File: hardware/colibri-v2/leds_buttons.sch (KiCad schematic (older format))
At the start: 39 parts, among them SW1 SW_PUSH, SW3 SW_PUSH, SW5 SW_PUSH

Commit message: Re-annotated schematic
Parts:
- gave numbers to parts that had none: 24
- renumbered C30 to C29, R35 to R36, R36 to R37, R37 to R38, R38 to R39

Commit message: Associated footprints for R and some of the C
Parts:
- C27, C28, C29, C30, C31, C32: footprint (none) -> Capacitors_SMD:C_0603
- R18, R19, R20, R21, R22, R23, R24, R25, R26, R27, R28, R29, R30, R31, R32, R33, R34, R35, R36, R37, R38, R39: footprint (none) -> Resistors_SMD:R_0603

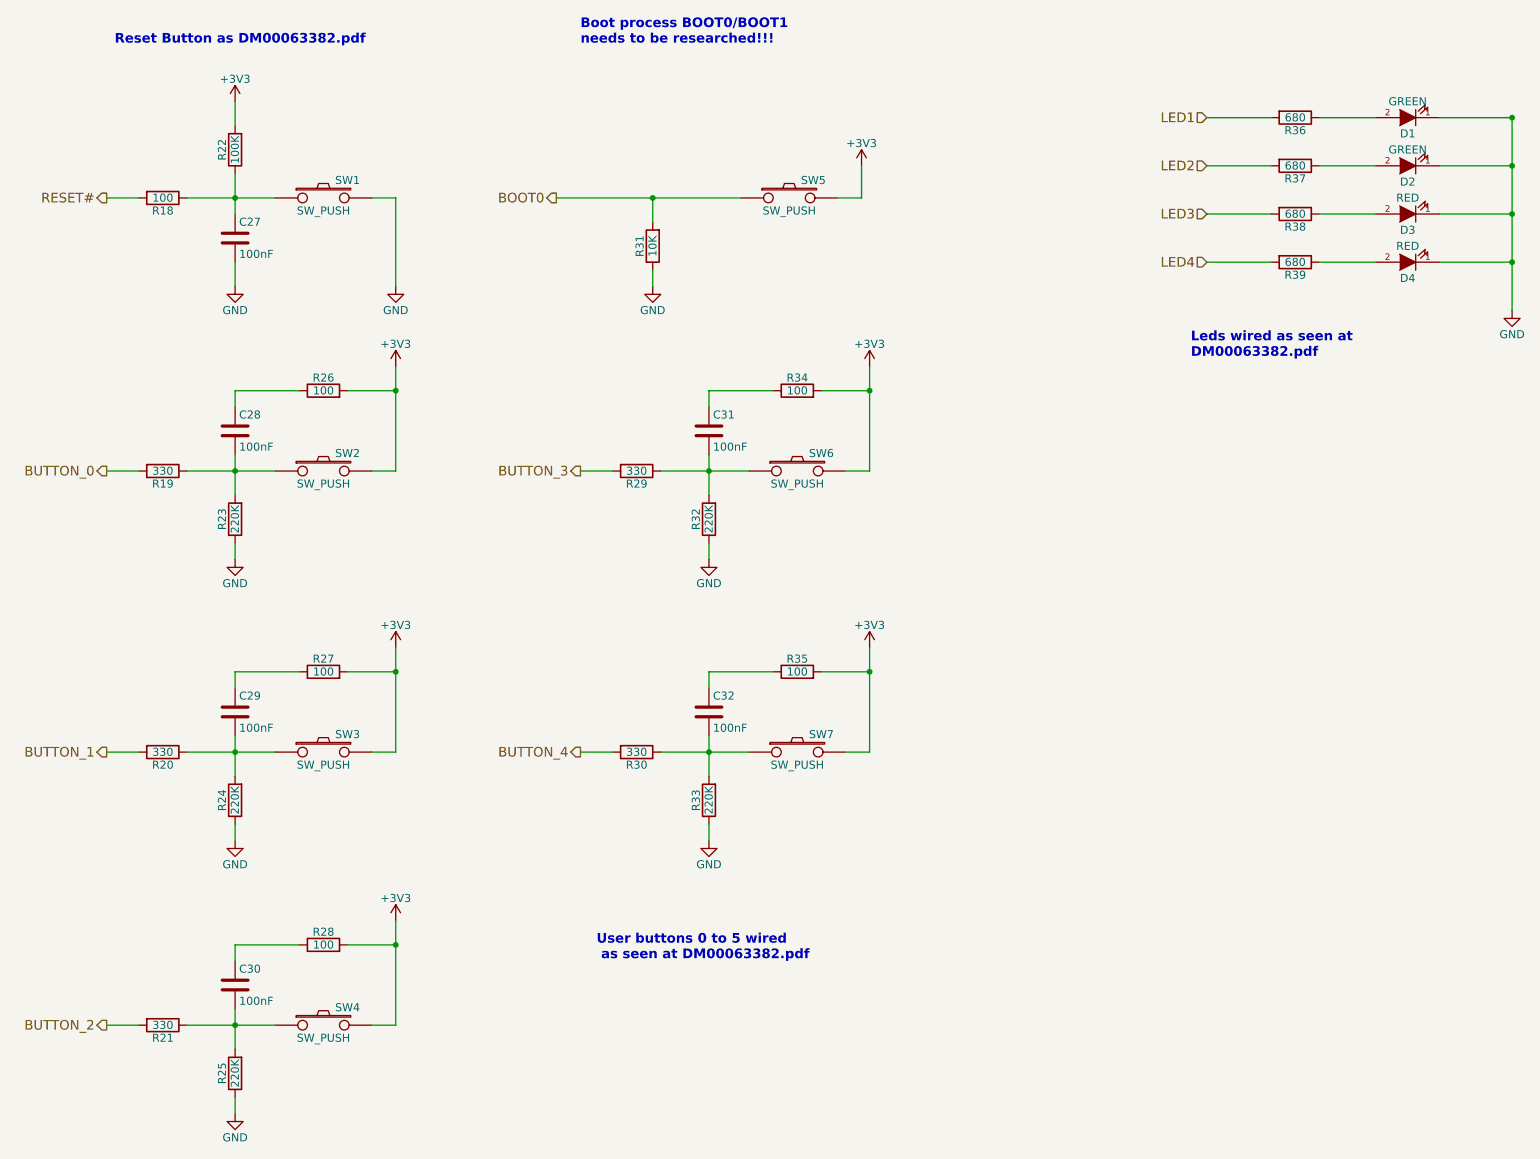
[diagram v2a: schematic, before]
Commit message: Work on JTAG and buttons sheets
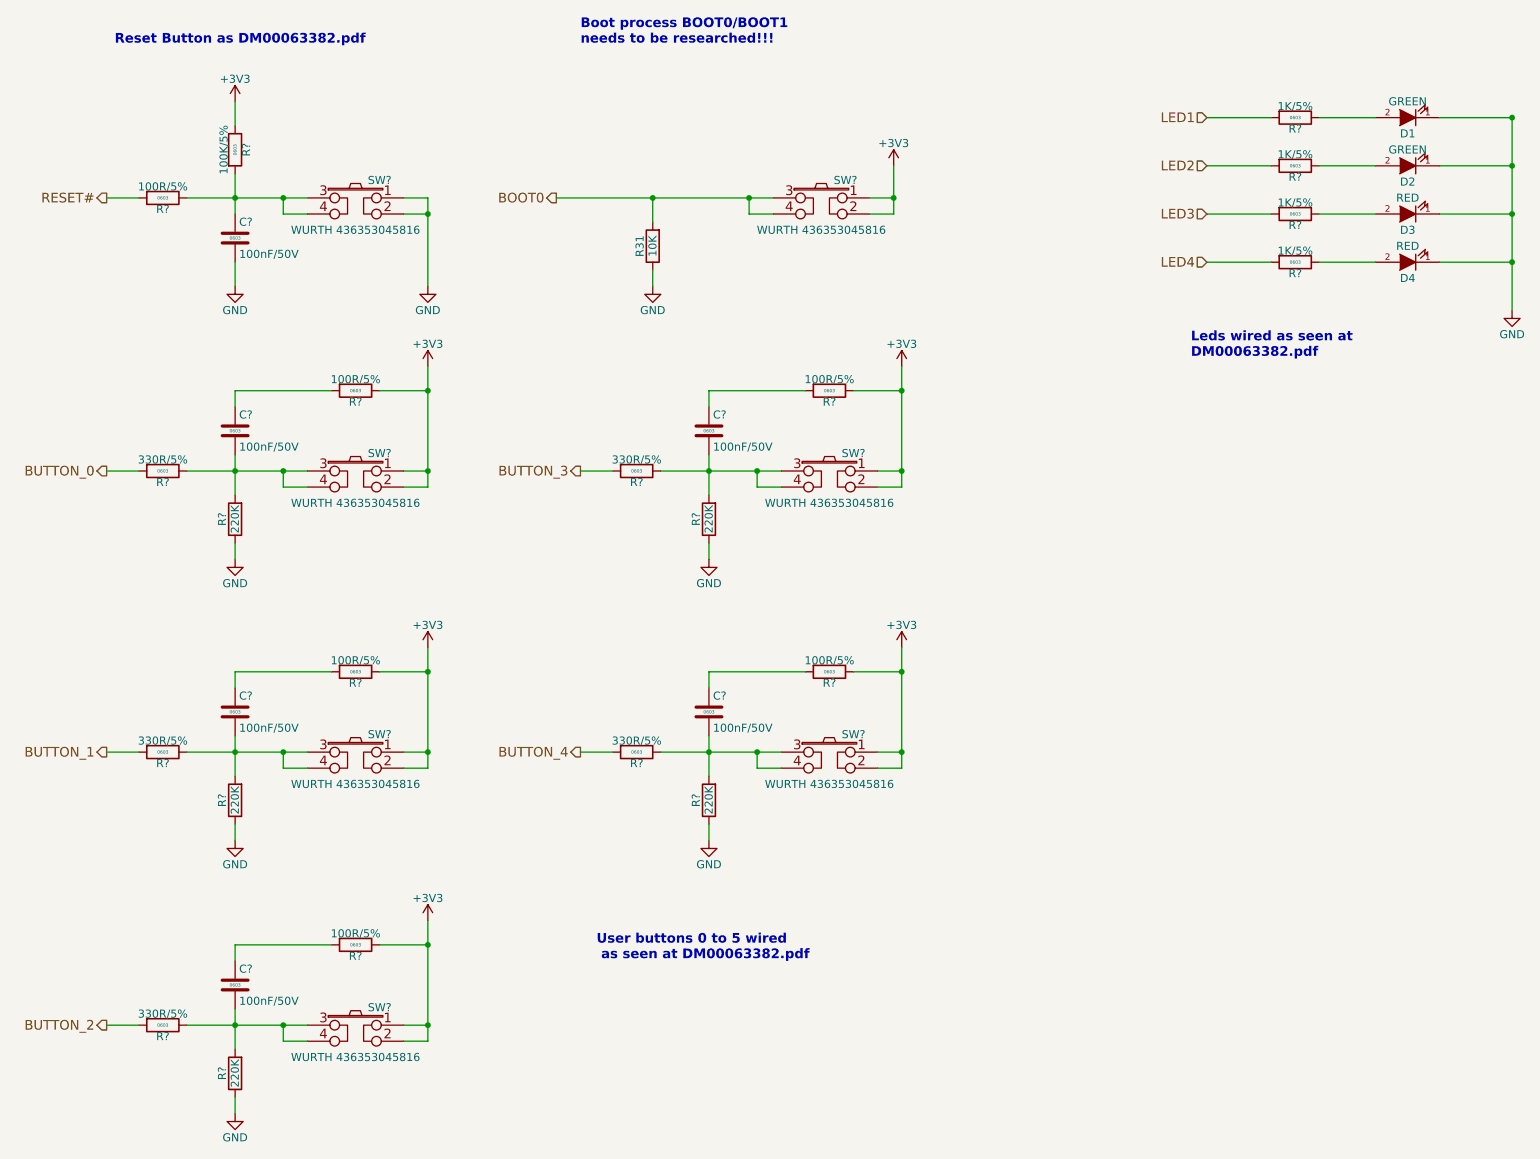
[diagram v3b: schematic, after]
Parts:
- removed C27, C28, C29, C30, C31, C32: 100nF, Capacitors_SMD:C_0603, symbol C
- removed R18, R26, R27, R28, R34, R35: 100, Resistors_SMD:R_0603, symbol R
- removed R19, R20, R21, R29, R30: 330, Resistors_SMD:R_0603, symbol R
- removed R22: 100K, Resistors_SMD:R_0603, symbol R
- removed R23, R24, R25, R32, R33: 220K, Resistors_SMD:R_0603, symbol R
- removed R36, R37, R38, R39: 680, Resistors_SMD:R_0603, symbol R
- removed SW1, SW2, SW3, SW4, SW5, SW6, SW7: SW_PUSH, symbol SW_PUSH
- added C? (x6): 100nF/50V, Capacitors_SMD:C_0603, symbol C_SMT
- added R?: 100K/5%, Resistors_SMD:R_0603, symbol R_SMT
- added R? (x6): 100R/5%, Resistors_SMD:R_0603, symbol R_SMT
- added R? (x5): 220K, Resistors_SMD:R_0603, symbol R
- added R? (x5): 330R/5%, Resistors_SMD:R_0603, symbol R_SMT
- added R? (x4): 1K/5%, Resistors_SMD:R_0603, symbol R_SMT
- added SW? (x7): WURTH 436353045816, symbol SW_PUSH_TACKTILE
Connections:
- net +3V3: now also R?.1, R?.1, R?.1, R?.1, R?.1, R?.1, SW?.1, SW?.1, SW?.1, SW?.1, SW?.1, SW?.1, SW?.2, SW?.2, SW?.2, SW?.2, SW?.2, SW?.2
- net BOOT0: now also SW?.3, SW?.4
- net BUTTON_0: now also R?.2
- net BUTTON_1: now also R?.2
- net BUTTON_2: now also R?.2
- net BUTTON_3: now also R?.2
- net BUTTON_4: now also R?.2
- net GND: now also C?.2, R?.1, R?.1, R?.1, R?.1, R?.1, SW?.1, SW?.2
- net LED1: now also R?.2
- net LED2: now also R?.2
- net LED3: now also R?.2
- net LED4: now also R?.2
- net RESET#: now also R?.2
- net at D1.2 (A): now also R?.1
- net at D2.2 (A): now also R?.1
- net at D3.2 (A): now also R?.1
- net at D4.2 (A): now also R?.1
- new net: C?.1, R?.1, R?.2, SW?.3, SW?.4
- new net: C?.2, R?.1, R?.2, SW?.3, SW?.4 (x5)
- new net: C?.1, R?.2 (x5)

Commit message: Work on cortex USB connection.
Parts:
- renumbered D1 to D?, D2 to D?, D3 to D?, D4 to D?, R31 to R?
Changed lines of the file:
@@
 RESET#
 $Comp
-L LED D1
+L LED D?
 U 1 1 55862ED2
 P 9450 1200
-F 0 "D1" H 9450 1300 50  0000 C CNN
+F 0 "D?" H 9450 1300 50  0000 C CNN
 F 1 "GREEN" H 9450 1100 50  0000 C CNN
 F 2 "" H 9450 1200 60  0001 C CNN
@@
 $EndComp
 $Comp
-L LED D2
+L LED D?
 U 1 1 55863115
 P 9450 1500
-F 0 "D2" H 9450 1600 50  0000 C CNN
+F 0 "D?" H 9450 1600 50  0000 C CNN
 F 1 "GREEN" H 9450 1400 50  0000 C CNN
 F 2 "" H 9450 1500 60  0001 C CNN
@@
 $EndComp
 $Comp
-L LED D3
+L LED D?
 U 1 1 55863212
 P 9450 1800
-F 0 "D3" H 9450 1900 50  0000 C CNN
+F 0 "D?" H 9450 1900 50  0000 C CNN
 F 1 "RED" H 9450 1700 50  0000 C CNN
 F 2 "" H 9450 1800 60  0001 C CNN
@@
 $EndComp
 $Comp
-L LED D4
+L LED D?
 U 1 1 558632D0
 P 9450 2100
-F 0 "D4" H 9450 2200 50  0000 C CNN
+F 0 "D?" H 9450 2200 50  0000 C CNN
 F 1 "RED" H 9450 2000 50  0000 C CNN
 F 2 "" H 9450 2100 60  0001 C CNN
@@
 LED4
 $Comp
-L GND #PWR018
+L GND #PWR?
 U 1 1 56074E25
 P 3350 2250
-F 0 "#PWR018" H 3350 2000 50  0001 C CNN
+F 0 "#PWR?" H 3350 2000 50  0001 C CNN
 F 1 "GND" H 3350 2100 50  0000 C CNN
 F 2 "" H 3350 2250 60  0000 C CNN
@@
 BOOT0
 $Comp
-L R R31
+L R R?
 U 1 1 5622C644
 P 4750 2000
-F 0 "R31" V 4830 2000 50  0000 C CNN
+F 0 "R?" V 4830 2000 50  0000 C CNN
 F 1 "10K" V 4750 2000 50  0000 C CNN
 F 2 "Resistors_SMD:R_0603" V 4680 2000 30  0001 C CNN
@@
 $EndComp
 $Comp
-L GND #PWR019
+L GND #PWR?
 U 1 1 5622D3C9
 P 4750 2250
-F 0 "#PWR019" H 4750 2000 50  0001 C CNN
+F 0 "#PWR?" H 4750 2000 50  0001 C CNN
 F 1 "GND" H 4750 2100 50  0000 C CNN
 F 2 "" H 4750 2250 60  0000 C CNN
@@
 	4750 2250 4750 2150
 $Comp
-L GND #PWR020
+L GND #PWR?
 U 1 1 5623679B
 P 10100 2400
-F 0 "#PWR020" H 10100 2150 50  0001 C CNN
+F 0 "#PWR?" H 10100 2150 50  0001 C CNN
 F 1 "GND" H 10100 2250 50  0000 C CNN
 F 2 "" H 10100 2400 60  0000 C CNN
@@
 User buttons 0 to 5 wired\n as seen at DM00063382.pdf
 $Comp
-L GND #PWR030
+L GND #PWR?
 U 1 1 5623AF84
 P 2150 2250
-F 0 "#PWR030" H 2150 2000 50  0001 C CNN
+F 0 "#PWR?" H 2150 2000 50  0001 C CNN
 F 1 "GND" H 2150 2100 50  0000 C CNN
 F 2 "" H 2150 2250 60  0000 C CNN
@@
 	2150 2100 2150 2250
 $Comp
-L +3V3 #PWR031
+L +3V3 #PWR?
 U 1 1 5623B9D5
 P 2150 1100
-F 0 "#PWR031" H 2150 950 50  0001 C CNN
+F 0 "#PWR?" H 2150 950 50  0001 C CNN
 F 1 "+3V3" H 2150 1240 50  0000 C CNN
 F 2 "" H 2150 1100 60  0000 C CNN
@@
 Reset Button as DM00063382.pdf
 $Comp
-L +3V3 #PWR032
+L +3V3 #PWR?
 U 1 1 5623E09E
 P 6250 1500
-F 0 "#PWR032" H 6250 1350 50  0001 C CNN
+F 0 "#PWR?" H 6250 1350 50  0001 C CNN
 F 1 "+3V3" H 6250 1640 50  0000 C CNN
 F 2 "" H 6250 1500 60  0000 C CNN
